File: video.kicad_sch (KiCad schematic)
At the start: 52 parts, among them IC103 HUC6260, IC108 μPC358C

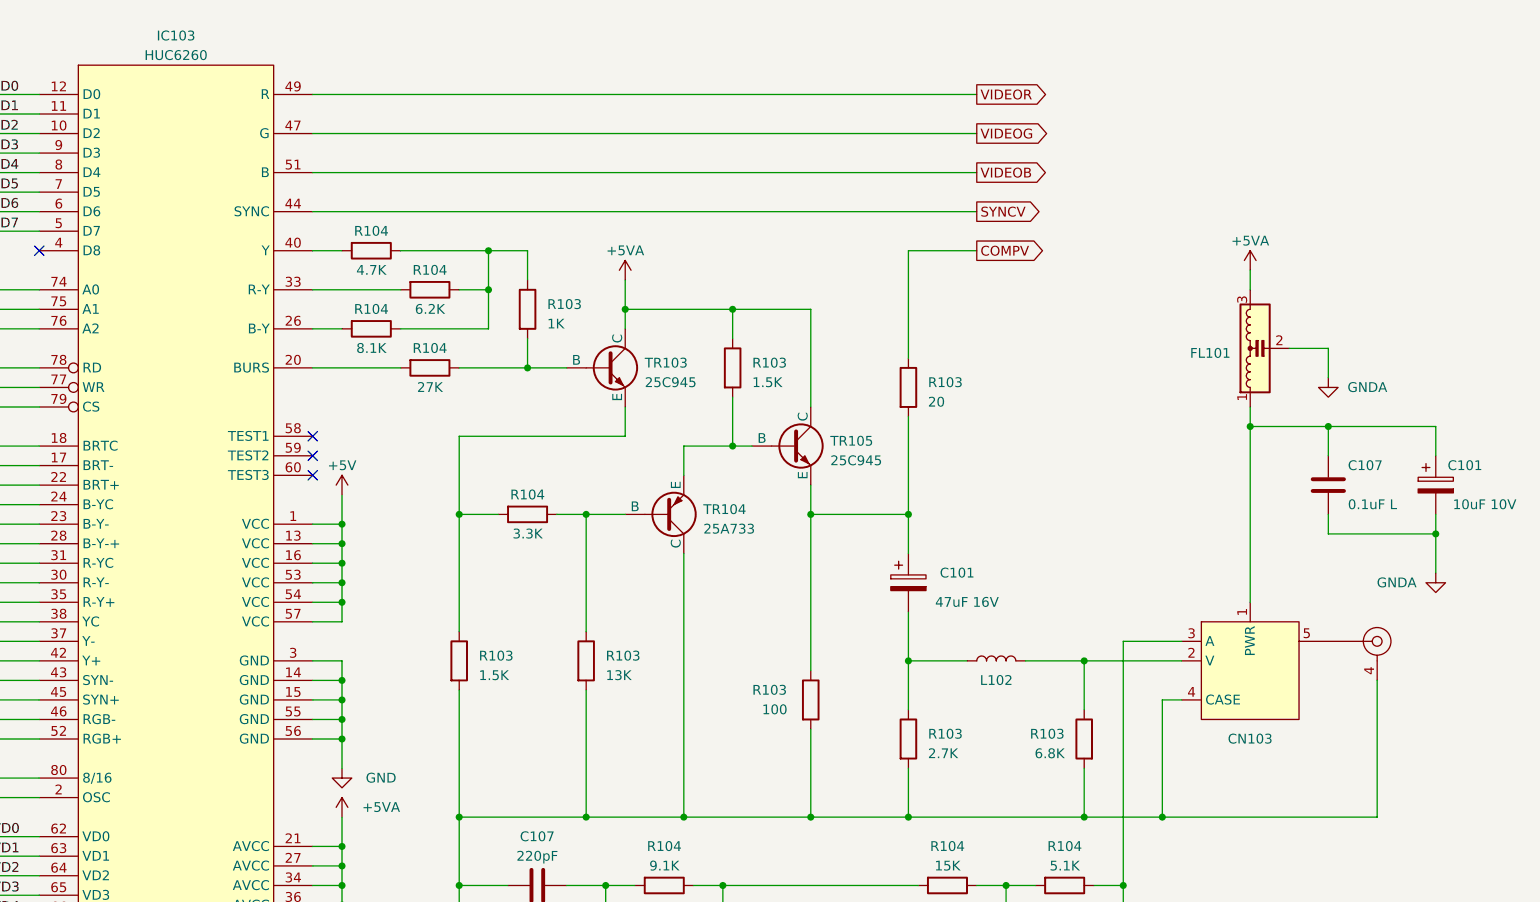
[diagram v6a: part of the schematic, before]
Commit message: Silkscreen stuff, tidy schematics, corrections.
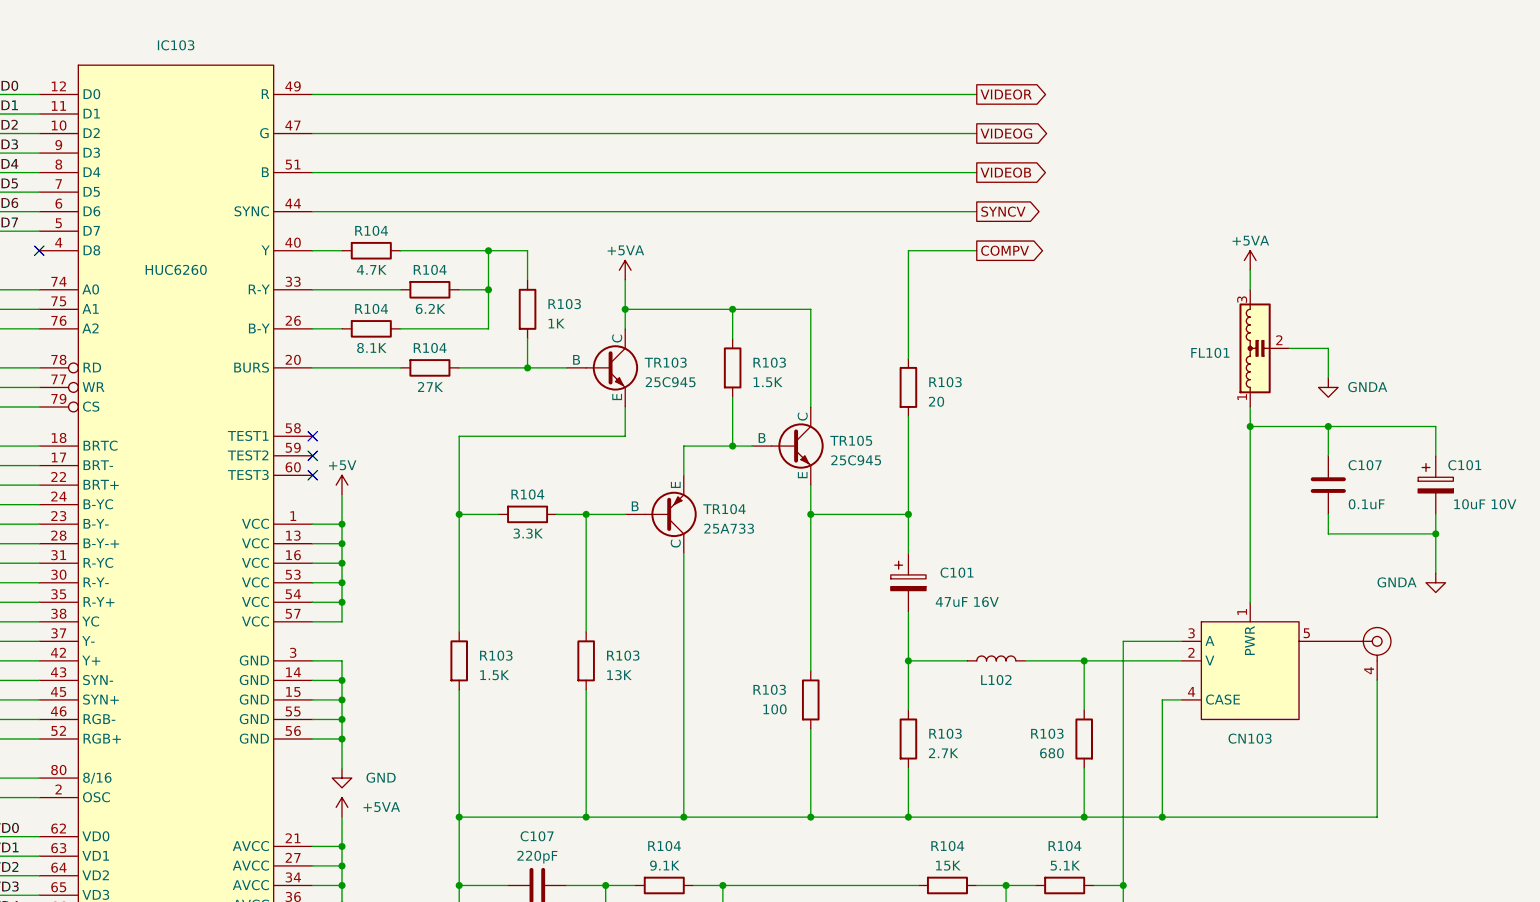
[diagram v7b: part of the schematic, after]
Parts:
- C107: value 0.1uF L -> 0.1uF
- R103: value 6.8K -> 680
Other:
- title: (none) -> PC Engine Video Encoding
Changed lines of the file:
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@@
 (kicad_sch (version 20230121) (generator eeschema)
   (paper "A3")
+  (title_block
+    (title "PC Engine Video Encoding")
+    (date "2023-08-17")
+    (rev "1.0")
+    (comment 1 "Differences reverse engineered from original PWD-623A board")
+    (comment 2 "Adapted from existing TurboGrafx-16 schematics by Cosam")
+  )
   (junction (at 210.82 144.78) (diameter 0) (color 0 0 0 0)
   )
@@
       (effects (font (size 1.27 1.27)) (justify right))
     )
-    (property "Value" "0.1uF L" (at 341.63 100.33 0)
+    (property "Value" "0.1uF" (at 341.63 100.33 0)
       (effects (font (size 1.27 1.27)) (justify right))
     )
@@
   )
   (symbol (lib_id "PC-Engine:Hu6260") (at 189.23 102.87 0) (unit 1)
-    (in_bom yes) (on_board yes) (dnp no) (fields_autoplaced)
-    (property "Reference" "IC103" (at 189.23 39.37 0)
-      (effects (font (size 1.27 1.27)))
-    )
-    (property "Value" "HUC6260" (at 189.23 41.91 0)
+    (in_bom yes) (on_board yes) (dnp no)
+    (property "Reference" "IC103" (at 189.23 40.64 0)
+      (effects (font (size 1.27 1.27)))
+    )
+    (property "Value" "HUC6260" (at 189.23 69.85 0)
       (effects (font (size 1.27 1.27)))
     )
@@
       (effects (font (size 1.27 1.27)) (justify left))
     )
-    (property "Value" "6.8K" (at 304.8 132.715 0)
+    (property "Value" "680" (at 304.8 132.715 0)
       (effects (font (size 1.27 1.27)) (justify left))
     )

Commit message: Silkscreen/DRC fixes
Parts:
- C107: footprint A-PCENGINE:SMD_1206 -> A-PCENGINE:SMD_1206_C
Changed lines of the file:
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@@
       (effects (font (size 1.27 1.27)) (justify right))
     )
-    (property "Footprint" "A-PCENGINE:SMD_1206" (at 338.1248 93.98 0)
+    (property "Footprint" "A-PCENGINE:SMD_1206_C" (at 338.1248 93.98 0)
       (effects (font (size 1.27 1.27)) hide)
     )
